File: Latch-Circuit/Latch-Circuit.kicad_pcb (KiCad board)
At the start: 2 copper layers, 90 x 50 mm, 96 parts, among them J1 BM02B-PASS-1-TF, J10 BM02B-PASS-1-TF, J2 BM03B-PASS-1-TF, J3 BM02B-PASS-1-TF, J4 BM02B-PASS-1-TF, J5 BM02B-PASS-1-TF, J6 BM02B-PASS-1-TF, J7 B2P-VH, J8 BM02B-PASS-1-TF, J9 BM02B-PASS-1-TF, K1 G5Q-1A4_DC12, K2 G5Q-1A4_DC12, K3 G5Q-1A4_DC12, Q1 DMP3098LQ-7, Q10 2N7002K-AU, Q11 2N7002K-AU, Q12 PJA3439-AU_R1_000A1, Q13 PJA3439-AU_R1_000A1, Q2 2N7002K-AU, Q3 PJA3439-AU_R1_000A1, Q4 2N7002K-AU, Q5 PJA3439-AU_R1_000A1, Q6 2N7002K-AU, Q7 2N7002K-AU, Q8 PJA3439-AU_R1_000A1, Q9 PJA3439-AU_R1_000A1

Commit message: ベタ修正
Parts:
- moved C11 0.50 mm to (48.0, 39.0)
- moved Q12 0.50 mm to (49.0, 31.5)
- moved R27 0.50 mm to (50.0, 39.0)
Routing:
- net GND: vias 439 -> 441

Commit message: 配置、配線終了
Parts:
- added D10: LED, LED_SMD:LED_0603_1608Metric, F.Cu at (50.2, 35.0)
- added D11: LED, LED_SMD:LED_0603_1608Metric, F.Cu at (50.2, 47.5)
- added D2: LED, LED_SMD:LED_0603_1608Metric, F.Cu at (4.25, 30.5)
- added D5: LED, LED_SMD:LED_0603_1608Metric, F.Cu at (50.2, 23.0)
- added Q10: 2N7002K-AU, ProjectEV:Package_SOT-23_2N7002K-AU, F.Cu at (47.5, 38.2)
- added Q15: 2N7002K-AU, ProjectEV:Package_SOT-23_2N7002K-AU, F.Cu at (53.5, 40.8)
- added Q2: 2N7002K-AU, ProjectEV:Package_SOT-23_2N7002K-AU, F.Cu at (47.5, 13.8)
- added Q3: 2N7002K-AU, ProjectEV:Package_SOT-23_2N7002K-AU, F.Cu at (53.5, 16.2)
- added Q6: 2N7002K-AU, ProjectEV:Package_SOT-23_2N7002K-AU, F.Cu at (47.5, 25.8)
- added Q9: 2N7002K-AU, ProjectEV:Package_SOT-23_2N7002K-AU, F.Cu at (53.5, 28.2)
- added R1: 100, Resistor_SMD:R_0603_1608Metric, F.Cu at (46.8, 19.0)
- added R12: 10k, Resistor_SMD:R_0603_1608Metric, F.Cu at (6.25, 28.8)
- added R14: 100, Resistor_SMD:R_0603_1608Metric, F.Cu at (46.8, 31.0)
- added R15: 100k, Resistor_SMD:R_0603_1608Metric, F.Cu at (47.5, 28.5)
- added R19: 100k, Resistor_SMD:R_0603_1608Metric, F.Cu at (44.8, 25.8)
- added R20: 100, Resistor_SMD:R_0603_1608Metric, F.Cu at (50.2, 26.2)
- added R22: 10k, Resistor_SMD:R_0603_1608Metric, F.Cu at (48.5, 21.5)
- added R24: 100, Resistor_SMD:R_0603_1608Metric, F.Cu at (46.8, 43.5)
- added R25: 100k, Resistor_SMD:R_0603_1608Metric, F.Cu at (47.5, 41.0)
- added R3: 100k, Resistor_SMD:R_0603_1608Metric, F.Cu at (47.5, 16.5)
- added R30: 100k, Resistor_SMD:R_0603_1608Metric, F.Cu at (44.8, 38.2)
- added R31: 100, Resistor_SMD:R_0603_1608Metric, F.Cu at (50.2, 38.8)
- added R4: 100k, Resistor_SMD:R_0603_1608Metric, F.Cu at (44.8, 13.8)
- added R47: 10k, Resistor_SMD:R_0603_1608Metric, F.Cu at (48.5, 33.5)
- added R48: 10k, Resistor_SMD:R_0603_1608Metric, F.Cu at (48.5, 46.0)
- added R5: 1M, Resistor_SMD:R_0603_1608Metric, F.Cu at (13.8, 25.0)
- added R7: 100, Resistor_SMD:R_0603_1608Metric, F.Cu at (50.2, 14.2)
- R16: renamed from R7; value 1M -> 100k
- R18: renamed from R9; value 1M -> 100k
- R28: renamed from R14; value 1M -> 100k
- R29: renamed from R15; value 1M -> 100k
- R32: renamed from R16; value 1M -> 100k
- R33: renamed from R17; value 1M -> 100k
- R39: renamed from R22; value 1M -> 100k
- R41: renamed from R24; value 1M -> 100k
- R42: renamed from R25; value 1M -> 100k
- R44: renamed from R27; value 1M -> 100k
- R8: renamed from R3; value 1M -> 100k
- R9: renamed from R4; value 1M -> 100k
- moved G*** 25.2 mm to (5.00, 36.0)
- moved C2 11.5 mm to (11.5, 25.2), turned to 90 degrees
- moved R2 10.7 mm to (3.75, 23.0), turned to -90 degrees
- moved R43 7.43 mm to (45.0, 44.0)
- moved R44 7.20 mm to (43.2, 41.5)
- moved Q1 7.07 mm to (6.50, 23.0), turned to 0 degrees
- moved R40 7.07 mm to (45.0, 31.5)
- moved Q19 7.04 mm to (42.2, 45.0)
- moved R17 7.00 mm to (45.0, 19.5)
- moved C11 6.96 mm to (41.5, 41.5)
- moved Q18 6.82 mm to (42.2, 32.5)
- moved R41 6.82 mm to (43.2, 29.0)
- moved C10 6.80 mm to (39.5, 45.0)
- moved Q8 6.77 mm to (42.2, 20.5)
- moved R18 6.75 mm to (43.2, 17.0)
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- renumbered D2 to D3, D3 to D4, D4 to D6, D5 to D7, D6 to D8, D7 to D9, Q6 to Q11, Q7 to Q12, Q8 to Q13, Q9 to Q14, Q10 to Q16, Q11 to Q17, Q12 to Q18, Q13 to Q19, Q2 to Q4, Q3 to Q5, Q4 to Q7, Q5 to Q8, R11 to R10, R5 to R11, R6 to R13, R8 to R17, R1 to R2, R10 to R21, R30 to R23, R12 to R26, R13 to R27, R18 to R34, R19 to R35, R31 to R36, R20 to R37, R21 to R38, R23 to R40, R26 to R43, R28 to R45, R29 to R46, R32 to R49, R2 to R6
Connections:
- J10 pad 2: GND -> /IMD_LED_K
- J8 pad 2: GND -> /AMS_LED_K
- J9 pad 2: GND -> /BSPD_LED_K
- R10 pad 2: /AMS_RELAY_DRIVE -> +12V
- R23 pad 2: /BSPD_RELAY_DRIVE -> +12V
- R36 pad 2: /IMD_RELAY_DRIVE -> +12V
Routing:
- net /IMD_RELAY_DRIVE: track 71.4 -> 31.6 mm, vias 1 -> 0
- net /IMD_LED_K: track 0.00 -> 36.7 mm
- net /BSPD_RELAY_DRIVE: track 60.3 -> 32.2 mm, vias 1 -> 2
- net /BSPD_LED_K: track 0.00 -> 27.6 mm, vias 0 -> 2
- net /AMS_RELAY_DRIVE: track 59.5 -> 32.2 mm, vias 0 -> 2
- net /AMS_LED_K: track 0.00 -> 26.9 mm, vias 0 -> 2
- net /SHDN_OUT: track 11.8 -> 0.00 mm
- net /IMD_STATUS: track 29.2 -> 39.9 mm
- net /TO_AMS_RST_SW: track 32.6 -> 22.0 mm, vias 0 -> 2
- net /TO_IMD_RST_SW: track 32.6 -> 22.3 mm, vias 0 -> 2
- net Net-(Q6-D): track 0.00 -> 5.85 mm
- net Net-(Q2-D): track 0.00 -> 5.85 mm
- net Net-(Q10-D): track 0.00 -> 5.85 mm
- net +12V: track 0.00 -> 4.41 mm, vias 22 -> 36
- net /TO_BSPD_RST_SW: track 32.5 -> 28.6 mm, vias 0 -> 2
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- added copper zone on F.Cu, net /AMS_RELAY_DRIVE
- added copper zone on F.Cu, net /BSPD_RELAY_DRIVE
- added copper zone on F.Cu, net /IMD_RELAY_DRIVE
- added copper zone on F.Cu, net /SHDN_IN
- added copper zone on F.Cu, net /SHDN_OUT
- added copper zone on F.Cu, net /TO_AMS_RST_SW
- added copper zone on F.Cu, net /TO_BSPD_RST_SW
- added copper zone on F.Cu, net /TO_IMD_RST_SW
- added copper zone on B.Cu, net Net-(C12-Pad1)
- added copper zone on F.Cu, net Net-(K1-Pad3)
- added copper zone on F.Cu, net Net-(K2-Pad3)
- removed copper zone on B.Cu, net /SHDN_IN
- removed copper zone on B.Cu, net /SHDN_OUT
- removed copper zone on B.Cu, net Net-(K1-Pad3)
- removed copper zone on B.Cu, net Net-(K2-Pad3)
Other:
- board text added: "Latch-Circuit-v1.1"
- board text removed: "Latch-Circuit-v1.0"

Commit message: complete AW, DRC next->select parts at JLCPCB
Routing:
- net GND: track 0.00 -> 16.3 mm, vias 95 -> 476

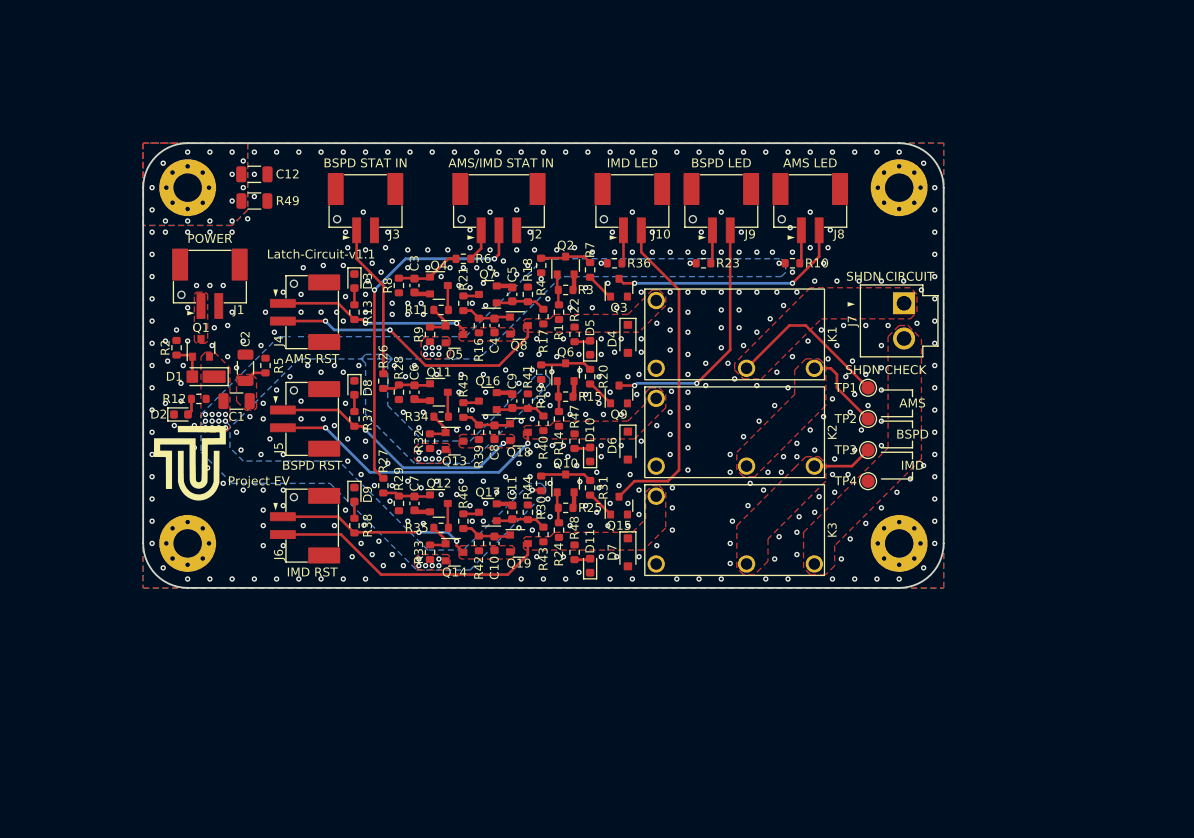
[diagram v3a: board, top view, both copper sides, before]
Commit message: add 捨て基板, Toolinghole, Fiducial
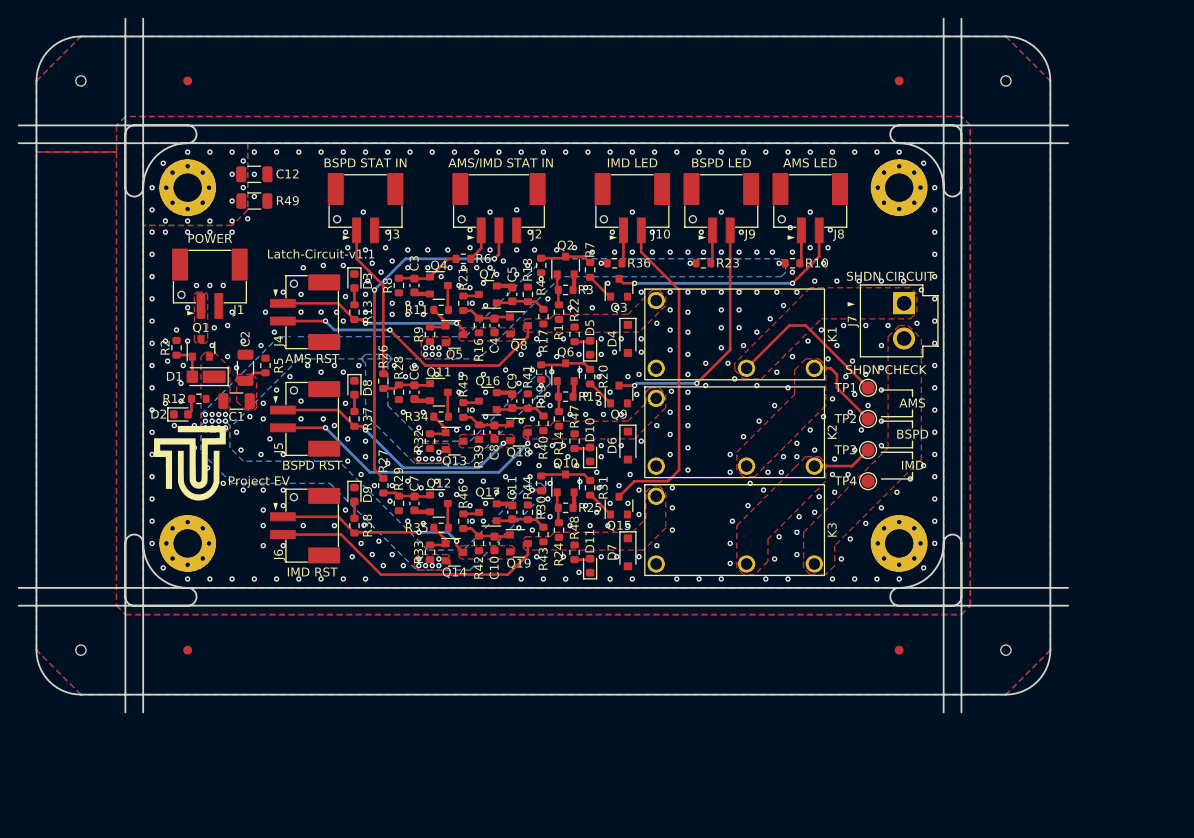
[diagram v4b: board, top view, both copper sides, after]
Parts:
- added REF**: Fiducial_JLCPCB, ProjectEV:Fiducial_JLCPCB, F.Cu at (85.0, -7.00)
- added REF**: ToolingHole_JLCPCB, ProjectEV:ToolingHole_JLCPCB, F.Cu at (97.0, -7.00)
- added REF**: Fiducial_JLCPCB, ProjectEV:Fiducial_JLCPCB, F.Cu at (85.0, 57.0)
- added REF**: ToolingHole_JLCPCB, ProjectEV:ToolingHole_JLCPCB, F.Cu at (-7.00, 57.0)
- added REF**: Fiducial_JLCPCB, ProjectEV:Fiducial_JLCPCB, F.Cu at (5.00, 57.0)
- added REF**: ToolingHole_JLCPCB, ProjectEV:ToolingHole_JLCPCB, F.Cu at (-7.00, -7.00)
- added REF**: ToolingHole_JLCPCB, ProjectEV:ToolingHole_JLCPCB, F.Cu at (97.0, 57.0)
- added REF**: Fiducial_JLCPCB, ProjectEV:Fiducial_JLCPCB, F.Cu at (5.00, -7.00)
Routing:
- added copper zone on B.Cu, net (none)
- added copper zone on F.Cu, net (none)
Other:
- board size 90 x 50 mm -> 118 x 78 mm
- board text added: "V-cut"

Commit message: 原点修正
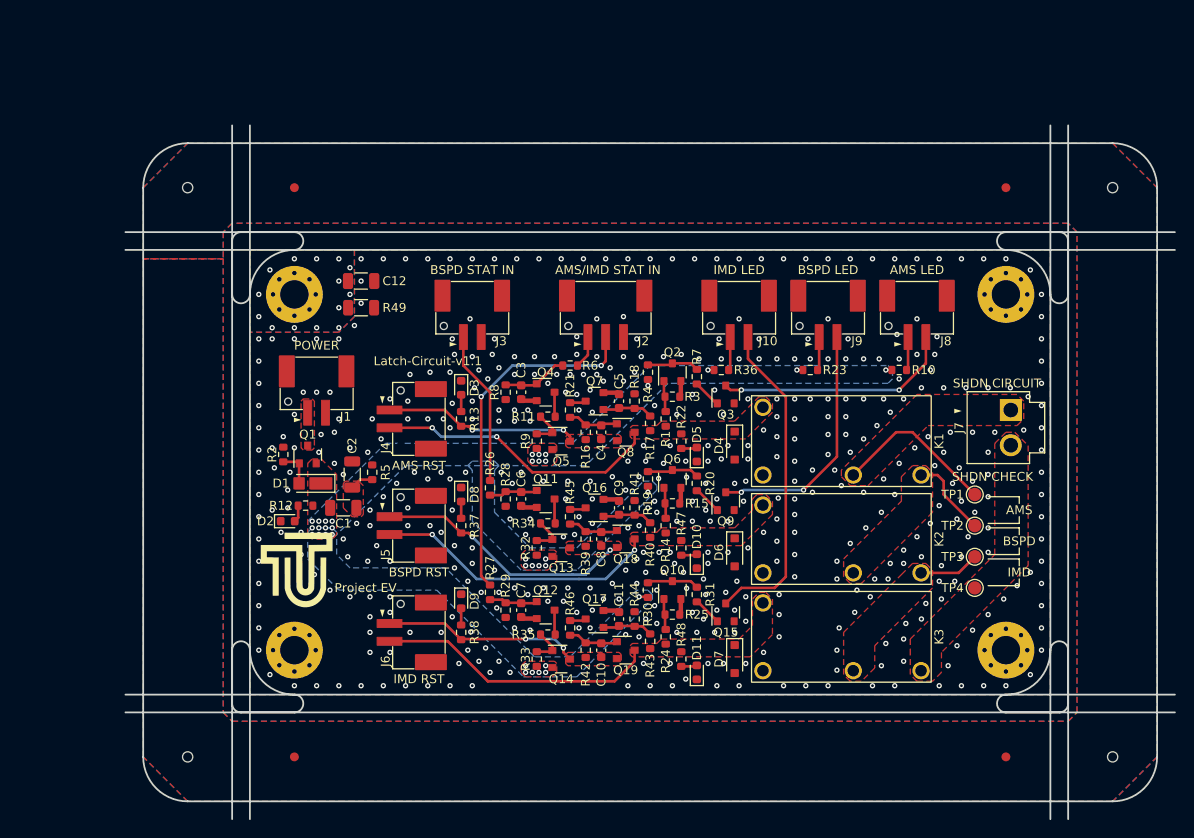
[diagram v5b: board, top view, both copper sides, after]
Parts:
- moved C1 17.0 mm to (22.5, 41.0)
- moved C10 17.0 mm to (51.5, 57.0)
- moved C11 17.0 mm to (53.5, 53.5)
- moved C12 17.0 mm to (24.5, 15.5)
- moved C2 17.0 mm to (23.5, 37.2)
- moved C3 17.0 mm to (42.5, 28.0)
- moved C4 17.0 mm to (51.5, 32.5)
- moved C5 17.0 mm to (53.5, 29.0)
- moved C6 17.0 mm to (42.5, 40.0)
- moved C7 17.0 mm to (42.5, 52.5)
- moved C8 17.0 mm to (51.5, 44.5)
- moved C9 17.0 mm to (53.5, 41.0)
- moved D1 17.0 mm to (18.8, 38.2)
- moved D10 17.0 mm to (62.2, 47.0)
- moved D11 17.0 mm to (62.2, 59.5)
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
